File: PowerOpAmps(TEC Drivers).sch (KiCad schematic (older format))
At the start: 5 parts

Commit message: working on second circuit
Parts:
- added C5, C6: 10u, symbol Device:C
- added C8: 0.1u, symbol Device:C
- added R3, R5, R6, R?: 470, symbol Device:R
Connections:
- net labels added: TEC_Minus, Temp_Ctrl_Output
- wire segments 26 -> 59
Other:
- moved on the sheet: U?
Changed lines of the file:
@@
-$Comp
-L OPA569AIDWPR:OPA569AIDWPR U?
-U 1 1 60C92272
-P 3700 1800
-F 0 "U?" H 5600 2187 60  0000 C CNN
-F 1 "OPA569AIDWPR" H 5600 2081 60  0000 C CNN
-F 2 "DWP20_4P32X3P81" H 5600 2040 60  0001 C CNN
-F 3 "" H 3700 1800 60  0000 C CNN
-	1    3700 1800
-	1    0    0    -1
-$EndComp
 $Comp
 L OPA569AIDWPR:OPA569AIDWPR U?
 U 1 1 60C94364
-P 3750 4350
-F 0 "U?" H 5650 4737 60  0000 C CNN
-F 1 "OPA569AIDWPR" H 5650 4631 60  0000 C CNN
-F 2 "DWP20_4P32X3P81" H 5650 4590 60  0001 C CNN
-F 3 "" H 3750 4350 60  0000 C CNN
-	1    3750 4350
+P 3700 4550
+F 0 "U?" H 5700 4100 60  0000 C CNN
+F 1 "OPA569AIDWPR" H 5700 3950 60  0000 C CNN
+F 2 "DWP20_4P32X3P81" H 5600 4790 60  0001 C CNN
+F 3 "" H 3700 4550 60  0000 C CNN
+	1    3700 4550
 	1    0    0    -1
 $EndComp
@@
 	3600 2000 3600 1800
 Connection ~ 3600 1800
-Wire Wire Line
-	3600 1800 3450 1800
 $Comp
 L power:GND #PWR?
@@
 	1    0    0    -1
 $EndComp
-Wire Wire Line
-	7500 2200 8150 2200
-Wire Wire Line
-	7500 2100 8150 2100
-Wire Wire Line
-	7500 1900 8150 1900
-Wire Wire Line
-	7500 2000 7650 2000
 Wire Wire Line
 	7650 2000 7650 1100
@@
 	8250 2600 8250 2800
 Wire Wire Line
-	7500 2400 9050 2400
+	7500 2400 8500 2400
+Text Label 7650 1100 0    50   ~ 0
+To_Arduino_AtoD
+Text Label 9450 2700 0    50   ~ 0
+To_4.2V_Supply
+Wire Wire Line
+	8000 2700 9450 2700
+Text Label 9050 2400 0    50   ~ 0
+TEC_Minus
+Wire Wire Line
+	8500 2400 8500 3400
+Wire Wire Line
+	8500 3400 7450 3400
+Wire Wire Line
+	3150 3400 3150 3650
+Wire Wire Line
+	3150 4950 3700 4950
+Connection ~ 8500 2400
+Wire Wire Line
+	8500 2400 9050 2400
+$Comp
+L Device:R R6
+U 1 1 60CA6672
+P 7150 3400
+F 0 "R6" V 6943 3400 50  0000 C CNN
+F 1 "470" V 7034 3400 50  0000 C CNN
+F 2 "" V 7080 3400 50  0001 C CNN
+F 3 "~" H 7150 3400 50  0001 C CNN
+	1    7150 3400
+	0    1    1    0
+$EndComp
+Wire Wire Line
+	7300 3650 7450 3650
+Wire Wire Line
+	7450 3650 7450 3400
+Connection ~ 7450 3400
+Wire Wire Line
+	7450 3400 7300 3400
+Wire Wire Line
+	3150 3400 6850 3400
+$Comp
+L Device:C C6
+U 1 1 60CADB61
+P 7150 3650
+F 0 "C6" V 7000 3600 50  0000 C CNN
+F 1 "10u" V 7000 3750 50  0000 C CNN
+F 2 "" H 7188 3500 50  0001 C CNN
+F 3 "~" H 7150 3650 50  0001 C CNN
+	1    7150 3650
+	0    1    1    0
+$EndComp
+Wire Wire Line
+	7000 3650 6850 3650
+Wire Wire Line
+	6850 3650 6850 3400
+Connection ~ 6850 3400
+Wire Wire Line
+	6850 3400 7000 3400
+Wire Wire Line
+	3150 3400 3150 2200
+Wire Wire Line
+	3150 2200 3700 2200
+Connection ~ 3150 3400
+$Comp
+L Device:R R5
+U 1 1 60CAF386
+P 3150 3800
+F 0 "R5" H 3080 3754 50  0000 R CNN
+F 1 "470" H 3080 3845 50  0000 R CNN
+F 2 "" V 3080 3800 50  0001 C CNN
+F 3 "~" H 3150 3800 50  0001 C CNN
+	1    3150 3800
+	-1   0    0    1
+$EndComp
+Wire Wire Line
+	3150 3950 3150 4150
+Wire Wire Line
+	7500 5150 7500 5250
+Wire Wire Line
+	7500 5250 7750 5250
+Wire Wire Line
+	7750 5250 7750 4150
+Wire Wire Line
+	7750 4150 3150 4150
+Connection ~ 7500 5250
+Connection ~ 3150 4150
+Wire Wire Line
+	3150 4150 3150 4250
+Wire Wire Line
+	2900 4700 2900 4850
+$Comp
+L Device:C C5
+U 1 1 60CB3BC7
+P 2900 4550
+F 0 "C5" H 3100 4500 50  0000 C CNN
+F 1 "10u" H 3100 4600 50  0000 C CNN
+F 2 "" H 2938 4400 50  0001 C CNN
+F 3 "~" H 2900 4550 50  0001 C CNN
+	1    2900 4550
+	-1   0    0    1
+$EndComp
+Wire Wire Line
+	2900 4400 2900 4250
+$Comp
+L Device:R R?
+U 1 1 60CB4975
+P 3150 4550
+F 0 "R?" H 3080 4504 50  0000 R CNN
+F 1 "470" H 3080 4595 50  0000 R CNN
+F 2 "" V 3080 4550 50  0001 C CNN
+F 3 "~" H 3150 4550 50  0001 C CNN
+	1    3150 4550
+	-1   0    0    1
+$EndComp
+Wire Wire Line
+	3150 4700 3150 4850
+Wire Wire Line
+	3150 4250 2900 4250
+Connection ~ 3150 4250
+Wire Wire Line
+	3150 4250 3150 4400
+Wire Wire Line
+	2900 4850 3150 4850
+Connection ~ 3150 4850
+Wire Wire Line
+	3150 4850 3150 4950
+Wire Wire Line
+	3150 4950 2500 4950
+Connection ~ 3150 4950
+$Comp
+L Device:R R3
+U 1 1 60CB799D
+P 2350 4950
+F 0 "R3" V 2143 4950 50  0000 C CNN
+F 1 "470" V 2234 4950 50  0000 C CNN
+F 2 "" V 2280 4950 50  0001 C CNN
+F 3 "~" H 2350 4950 50  0001 C CNN
+	1    2350 4950
+	0    1    1    0
+$EndComp
+Wire Wire Line
+	2200 4950 1300 4950
+Text Label 1300 4950 0    50   ~ 0
+Temp_Ctrl_Output
+Wire Wire Line
+	3700 2300 3550 2300
+Wire Wire Line
+	3550 2300 3550 3200
+Wire Wire Line
+	3550 5050 3700 5050
+$Comp
+L Device:C C8
+U 1 1 60CB9EEA
+P 3700 3200
+F 0 "C8" V 3550 3100 50  0000 L CNN
+F 1 "0.1u" V 3550 3250 50  0000 L CNN
+F 2 "" H 3738 3050 50  0001 C CNN
+F 3 "~" H 3700 3200 50  0001 C CNN
+	1    3700 3200
+	0    1    1    0
+$EndComp
+Connection ~ 3550 3200
+Wire Wire Line
+	3550 3200 3550 5050
 Connection ~ 7500 2400
-Text Label 7400 1050 0    50   ~ 0
-To_Arduino_AtoD
-Text Label 9600 2700 0    50   ~ 0
-To_4.2V_Supply
-Wire Wire Line
-	8000 2700 9450 2700
+Wire Wire Line
+	3600 1800 3450 1800
+$Comp
+L OPA569AIDWPR:OPA569AIDWPR U?
+U 1 1 60C92272
+P 3700 1800
+F 0 "U?" H 5650 1350 60  0000 C CNN
+F 1 "OPA569AIDWPR" H 5650 1250 60  0000 C CNN
+F 2 "DWP20_4P32X3P81" H 5600 2040 60  0001 C CNN
+F 3 "" H 3700 1800 60  0000 C CNN
+	1    3700 1800
+	1    0    0    -1
+$EndComp
+$Comp
+L power:GND #PWR?
+U 1 1 60CB8330
+P 3700 2700
+F 0 "#PWR?" H 3700 2450 50  0001 C CNN
+F 1 "GND" H 3705 2527 50  0000 C CNN
+F 2 "" H 3700 2700 50  0001 C CNN
+F 3 "" H 3700 2700 50  0001 C CNN
+	1    3700 2700
+	1    0    0    -1
+$EndComp
+Wire Wire Line
+	7500 1900 8150 1900
+Wire Wire Line
+	7500 2000 7650 2000
+Wire Wire Line
+	7500 2100 8150 2100
+Wire Wire Line
+	7500 2200 8150 2200
+$Comp
+L power:GND #PWR?
+U 1 1 60CBC7D5
+P 3850 3200
+F 0 "#PWR?" H 3850 2950 50  0001 C CNN
+F 1 "GND" H 3855 3027 50  0000 C CNN
+F 2 "" H 3850 3200 50  0001 C CNN
+F 3 "" H 3850 3200 50  0001 C CNN
+	1    3850 3200
+	1    0    0    -1
+$EndComp
 $EndSCHEMATC

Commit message: powerOpAmpBoard ready for QA
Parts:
- added C2: 100u, symbol Device:C
- added C4, C7: 0.1u, symbol Device:C
- added R10: 10k, symbol Device:R
- added R2: 470, symbol Device:R
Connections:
- net GND: now also U?.1 (POWERPAD), U?.10 (POWERPAD), U?.11 (POWERPAD), U?.12 (V+), U?.17 (V-), U?.18 (V-), U?.20 (POWERPAD), U?.3 (CURRENTLIMITSET), C2.1, C4.1, C4.2, C7.1, R10.2, R2.1
- net Output_of_2.5V_Reference: now reaches C8.2, U?.6 (IN+), U?.6 (IN+)
- net Output_of_2.5V_Reference: now also C7.2
- net Enable_Signal_from_Arduino_D5: now reaches U?.8 (ENABLE)
- net Enable_Signal_from_Arduino_D5: now also U?.8 (ENABLE), R10.1
- net at U?.13 (V+): now also C2.2
- net TEC_Plus: now reaches C5.2, R5.1, R?.2, U?.14 (VO), U?.15 (VO)
- net To_Arduino_AtoD_(pos-current-monitor): now reaches U?.19 (IMONITOR)
- net To_Arduino_AtoD_(pos-current-monitor): now also R2.2
- net To_Arduino_AtoD renamed To_Arduino_AtoD_(neg-current-monitor)
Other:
- moved on the sheet: C5, C8, R3, R5, R?

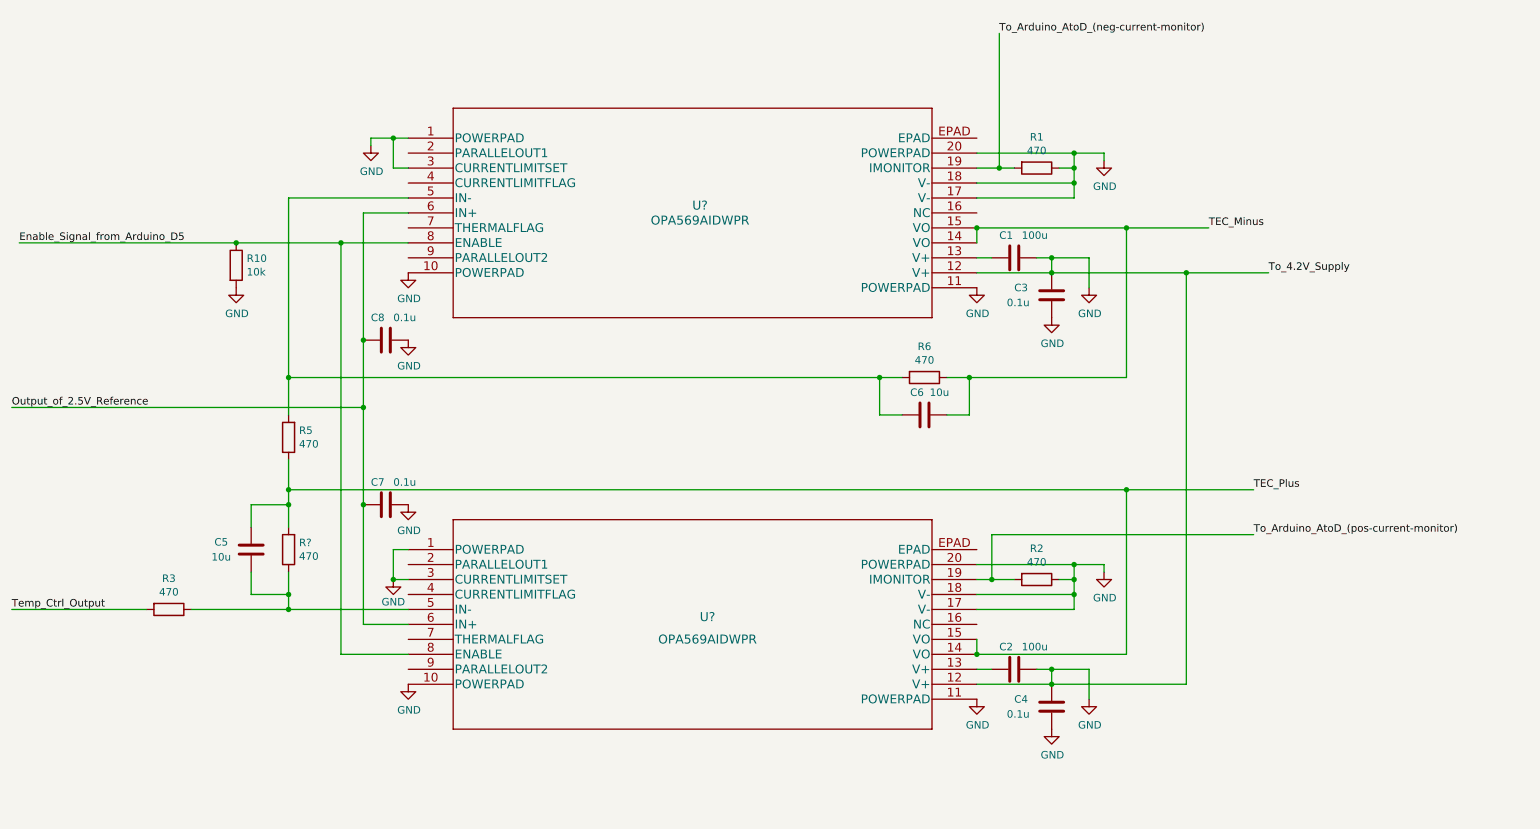
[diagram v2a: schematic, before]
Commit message: added capacitors on power op amp schematic
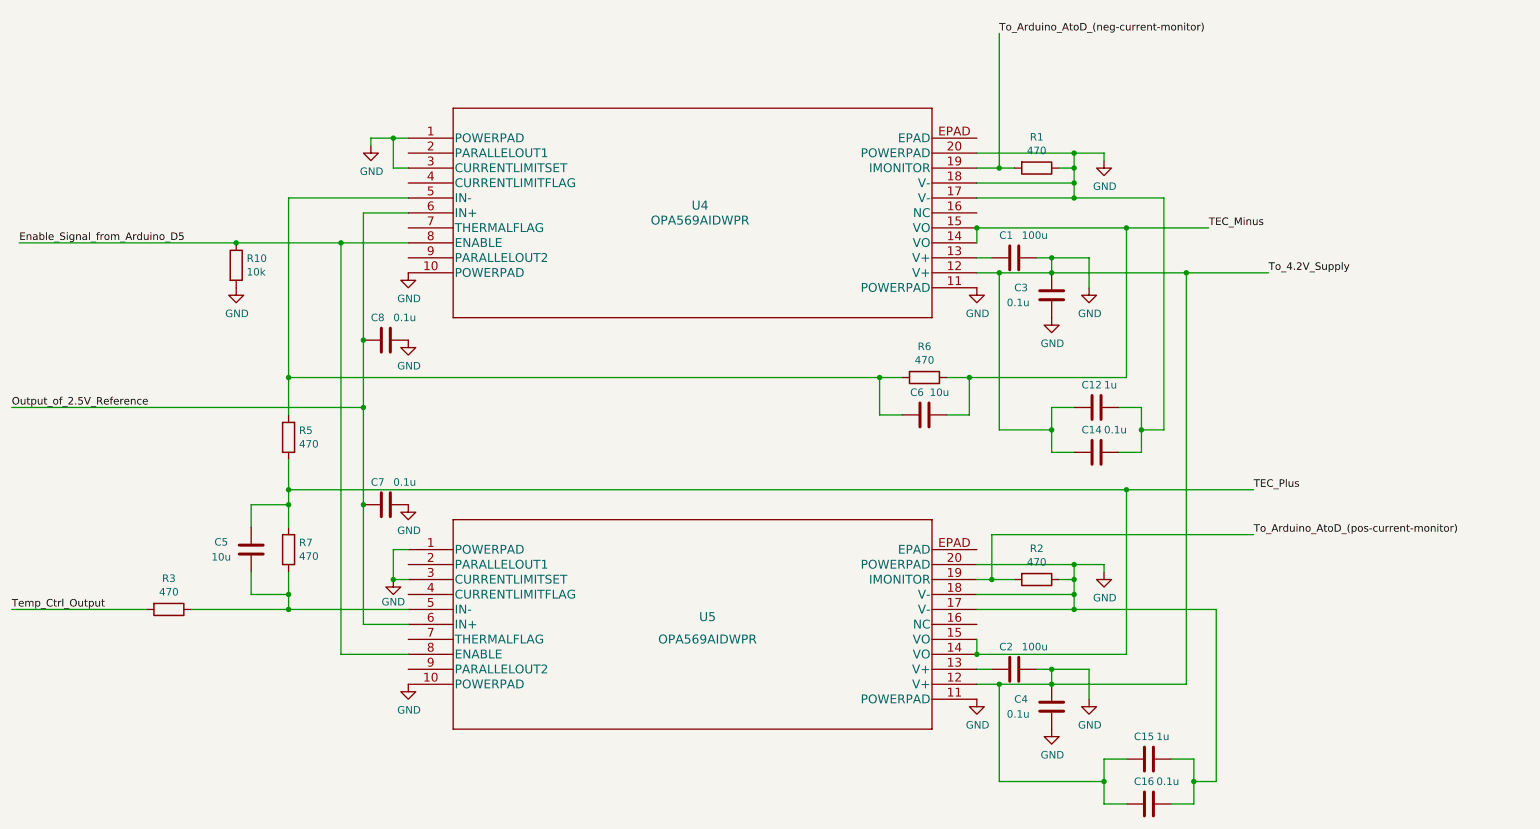
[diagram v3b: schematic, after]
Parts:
- added C12, C15: 1u, symbol Device:C
- added C14, C16: 0.1u, symbol Device:C
- gave numbers to parts that had none: 3
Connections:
- net GND: now also C12.1, C12.2, C14.1, C14.2, C15.1, C15.2, C16.1, C16.2
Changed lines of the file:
@@
 $EndDescr
 $Comp
-L OPA569AIDWPR:OPA569AIDWPR U?
+L OPA569AIDWPR:OPA569AIDWPR U5
 U 1 1 60C94364
 P 3700 4550
-F 0 "U?" H 5700 4100 60  0000 C CNN
+F 0 "U5" H 5700 4100 60  0000 C CNN
 F 1 "OPA569AIDWPR" H 5700 3950 60  0000 C CNN
 F 2 "DWP20_4P32X3P81" H 5600 4790 60  0001 C CNN
@@
 Connection ~ 3600 1800
 $Comp
-L power:GND #PWR?
+L power:GND #PWR018
 U 1 1 60C996D8
 P 3450 1850
-F 0 "#PWR?" H 3450 1600 50  0001 C CNN
+F 0 "#PWR018" H 3450 1600 50  0001 C CNN
 F 1 "GND" H 3455 1677 50  0000 C CNN
 F 2 "" H 3450 1850 50  0001 C CNN
@@
 	8150 2100 8150 2000
 $Comp
-L power:GND #PWR?
+L power:GND #PWR030
 U 1 1 60C9A1CF
 P 8350 1950
-F 0 "#PWR?" H 8350 1700 50  0001 C CNN
+F 0 "#PWR030" H 8350 1700 50  0001 C CNN
 F 1 "GND" H 8355 1777 50  0000 C CNN
 F 2 "" H 8350 1950 50  0001 C CNN
@@
 	7500 2500 7500 2400
 Wire Wire Line
-	7500 2700 8000 2700
-Wire Wire Line
 	7500 2600 7600 2600
 Wire Wire Line
@@
 Connection ~ 8000 2600
 $Comp
-L power:GND #PWR?
+L power:GND #PWR026
 U 1 1 60C9E215
 P 8000 3000
-F 0 "#PWR?" H 8000 2750 50  0001 C CNN
+F 0 "#PWR026" H 8000 2750 50  0001 C CNN
 F 1 "GND" H 8005 2827 50  0000 C CNN
 F 2 "" H 8000 3000 50  0001 C CNN
@@
 $EndComp
 $Comp
-L power:GND #PWR?
+L power:GND #PWR028
 U 1 1 60C9E30F
 P 8250 2800
-F 0 "#PWR?" H 8250 2550 50  0001 C CNN
+F 0 "#PWR028" H 8250 2550 50  0001 C CNN
 F 1 "GND" H 8255 2627 50  0000 C CNN
 F 2 "" H 8250 2800 50  0001 C CNN
@@
 Connection ~ 8000 2700
 $Comp
-L power:GND #PWR?
+L power:GND #PWR024
 U 1 1 60C9EDCF
 P 7500 2800
-F 0 "#PWR?" H 7500 2550 50  0001 C CNN
+F 0 "#PWR024" H 7500 2550 50  0001 C CNN
 F 1 "GND" H 7505 2627 50  0000 C CNN
 F 2 "" H 7500 2800 50  0001 C CNN
@@
 	2650 4400 2650 4250
 $Comp
-L Device:R R?
+L Device:R R7
 U 1 1 60CB4975
 P 2900 4550
-F 0 "R?" H 2830 4504 50  0000 R CNN
+F 0 "R7" H 2830 4504 50  0000 R CNN
 F 1 "470" H 2830 4595 50  0000 R CNN
 F 2 "" V 2830 4550 50  0001 C CNN
@@
 	3600 1800 3450 1800
 $Comp
-L OPA569AIDWPR:OPA569AIDWPR U?
+L OPA569AIDWPR:OPA569AIDWPR U4
 U 1 1 60C92272
 P 3700 1800
-F 0 "U?" H 5650 1350 60  0000 C CNN
+F 0 "U4" H 5650 1350 60  0000 C CNN
 F 1 "OPA569AIDWPR" H 5650 1250 60  0000 C CNN
 F 2 "DWP20_4P32X3P81" H 5600 2040 60  0001 C CNN
@@
 $EndComp
 $Comp
-L power:GND #PWR?
+L power:GND #PWR020
 U 1 1 60CB8330
 P 3700 2700
-F 0 "#PWR?" H 3700 2450 50  0001 C CNN
+F 0 "#PWR020" H 3700 2450 50  0001 C CNN
 F 1 "GND" H 3705 2527 50  0000 C CNN
 F 2 "" H 3700 2700 50  0001 C CNN
@@
 	7500 2200 8150 2200
 $Comp
-L power:GND #PWR?
+L power:GND #PWR021
 U 1 1 60CBC7D5
 P 3700 3150
-F 0 "#PWR?" H 3700 2900 50  0001 C CNN
+F 0 "#PWR021" H 3700 2900 50  0001 C CNN
 F 1 "GND" H 3705 2977 50  0000 C CNN
 F 2 "" H 3700 3150 50  0001 C CNN
@@
 $EndComp
 $Comp
-L power:GND #PWR?
+L power:GND #PWR022
 U 1 1 60C85B5A
 P 3700 4250
-F 0 "#PWR?" H 3700 4000 50  0001 C CNN
+F 0 "#PWR022" H 3700 4000 50  0001 C CNN
 F 1 "GND" H 3705 4077 50  0000 C CNN
 F 2 "" H 3700 4250 50  0001 C CNN
@@
 Output_of_2.5V_Reference
 Wire Wire Line
-	7500 5450 8000 5450
-Wire Wire Line
 	7500 5350 7600 5350
 Wire Wire Line
@@
 Connection ~ 8000 5350
 $Comp
-L power:GND #PWR?
+L power:GND #PWR027
 U 1 1 60C89B9A
 P 8000 5750
-F 0 "#PWR?" H 8000 5500 50  0001 C CNN
+F 0 "#PWR027" H 8000 5500 50  0001 C CNN
 F 1 "GND" H 8005 5577 50  0000 C CNN
 F 2 "" H 8000 5750 50  0001 C CNN
@@
 $EndComp
 $Comp
-L power:GND #PWR?
+L power:GND #PWR029
 U 1 1 60C89BA4
 P 8250 5550
-F 0 "#PWR?" H 8250 5300 50  0001 C CNN
+F 0 "#PWR029" H 8250 5300 50  0001 C CNN
 F 1 "GND" H 8255 5377 50  0000 C CNN
 F 2 "" H 8250 5550 50  0001 C CNN
@@
 	8900 5450 8900 2700
 $Comp
-L power:GND #PWR?
+L power:GND #PWR025
 U 1 1 60C94EDB
 P 7500 5550
-F 0 "#PWR?" H 7500 5300 50  0001 C CNN
+F 0 "#PWR025" H 7500 5300 50  0001 C CNN
 F 1 "GND" H 7505 5377 50  0000 C CNN
 F 2 "" H 7500 5550 50  0001 C CNN
@@
 	8150 4850 8150 4750
 $Comp
-L power:GND #PWR?
+L power:GND #PWR031
 U 1 1 60C9936E
 P 8350 4700
-F 0 "#PWR?" H 8350 4450 50  0001 C CNN
+F 0 "#PWR031" H 8350 4450 50  0001 C CNN
 F 1 "GND" H 8355 4527 50  0000 C CNN
 F 2 "" H 8350 4700 50  0001 C CNN
@@
 	3600 4750 3600 4550
 $Comp
-L power:GND #PWR?
+L power:GND #PWR019
 U 1 1 60CA4B15
 P 3600 4750
-F 0 "#PWR?" H 3600 4500 50  0001 C CNN
+F 0 "#PWR019" H 3600 4500 50  0001 C CNN
 F 1 "GND" H 3600 4600 50  0000 C CNN
 F 2 "" H 3600 4750 50  0001 C CNN
@@
 	2550 2500 1100 2500
 $Comp
-L power:GND #PWR?
+L power:GND #PWR017
 U 1 1 60CB8F3D
 P 2550 2800
-F 0 "#PWR?" H 2550 2550 50  0001 C CNN
+F 0 "#PWR017" H 2550 2550 50  0001 C CNN
 F 1 "GND" H 2555 2627 50  0000 C CNN
 F 2 "" H 2550 2800 50  0001 C CNN
@@
 $EndComp
 $Comp
-L power:GND #PWR?
+L power:GND #PWR023
 U 1 1 60CB936E
 P 3700 5450
-F 0 "#PWR?" H 3700 5200 50  0001 C CNN
+F 0 "#PWR023" H 3700 5200 50  0001 C CNN
 F 1 "GND" H 3705 5277 50  0000 C CNN
 F 2 "" H 3700 5450 50  0001 C CNN
@@
 	2900 4150 8500 4150
 Connection ~ 8500 4150
+Wire Wire Line
+	7500 5450 7650 5450
+Wire Wire Line
+	7650 5450 7650 6100
+Wire Wire Line
+	7650 6100 8350 6100
+Wire Wire Line
+	8350 6100 8350 5950
+Wire Wire Line
+	8350 5950 8500 5950
+Connection ~ 7650 5450
+Wire Wire Line
+	7650 5450 8000 5450
+$Comp
+L Device:C C15
+U 1 1 60CD3EBB
+P 8650 5950
+F 0 "C15" V 8500 5850 50  0000 L CNN
+F 1 "1u" V 8500 6000 50  0000 L CNN
+F 2 "" H 8688 5800 50  0001 C CNN
+F 3 "~" H 8650 5950 50  0001 C CNN
+	1    8650 5950
+	0    1    1    0
+$EndComp
+$Comp
+L Device:C C16
+U 1 1 60CD4799
+P 8650 6250
+F 0 "C16" V 8500 6150 50  0000 L CNN
+F 1 "0.1u" V 8500 6300 50  0000 L CNN
+F 2 "" H 8688 6100 50  0001 C CNN
+F 3 "~" H 8650 6250 50  0001 C CNN
+	1    8650 6250
+	0    1    1    0
+$EndComp
+Wire Wire Line
+	8500 6250 8350 6250
+Wire Wire Line
+	8350 6250 8350 6100
+Connection ~ 8350 6100
+Wire Wire Line
+	8800 6250 8950 6250
+Wire Wire Line
+	8950 6250 8950 6100
+Wire Wire Line
+	8950 6100 9100 6100
+Wire Wire Line
+	9100 6100 9100 4950
+Wire Wire Line
+	9100 4950 8150 4950
+Connection ~ 8150 4950
+Wire Wire Line
+	8800 5950 8950 5950
+Wire Wire Line
+	8950 5950 8950 6100
+Connection ~ 8950 6100
+Wire Wire Line
+	8000 3750 8000 3600
+Wire Wire Line
+	8000 3600 8150 3600
+$Comp
+L Device:C C12
+U 1 1 60CDE792
+P 8300 3600
+F 0 "C12" V 8150 3500 50  0000 L CNN
+F 1 "1u" V 8150 3650 50  0000 L CNN
+F 2 "" H 8338 3450 50  0001 C CNN
+F 3 "~" H 8300 3600 50  0001 C CNN
+	1    8300 3600
+	0    1    1    0
+$EndComp
+$Comp
+L Device:C C14
+U 1 1 60CDE79C
+P 8300 3900
+F 0 "C14" V 8150 3800 50  0000 L CNN
+F 1 "0.1u" V 8150 3950 50  0000 L CNN
+F 2 "" H 8338 3750 50  0001 C CNN
+F 3 "~" H 8300 3900 50  0001 C CNN
+	1    8300 3900
+	0    1    1    0
+$EndComp
+Wire Wire Line
+	8150 3900 8000 3900
+Wire Wire Line
+	8000 3900 8000 3750
+Connection ~ 8000 3750
+Wire Wire Line
+	8450 3900 8600 3900
+Wire Wire Line
+	8600 3900 8600 3750
+Wire Wire Line
+	8600 3750 8750 3750
+Wire Wire Line
+	8450 3600 8600 3600
+Wire Wire Line
+	8600 3600 8600 3750
+Connection ~ 8600 3750
+Wire Wire Line
+	7650 3750 7650 2700
+Wire Wire Line
+	7500 2700 7650 2700
+Wire Wire Line
+	7650 3750 8000 3750
+Connection ~ 7650 2700
+Wire Wire Line
+	7650 2700 8000 2700
+Wire Wire Line
+	8750 2200 8150 2200
+Wire Wire Line
+	8750 2200 8750 3750
+Connection ~ 8150 2200
 $EndSCHEMATC
